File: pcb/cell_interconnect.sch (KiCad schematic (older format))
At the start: 24 parts, among them J1 C0, J10 Taps 6-8, J11 Taps 0-5, J2 C1, J3 C2, J4 C3, J5 C4, J6 C5, J7 C6, J8 C7, J9 C8

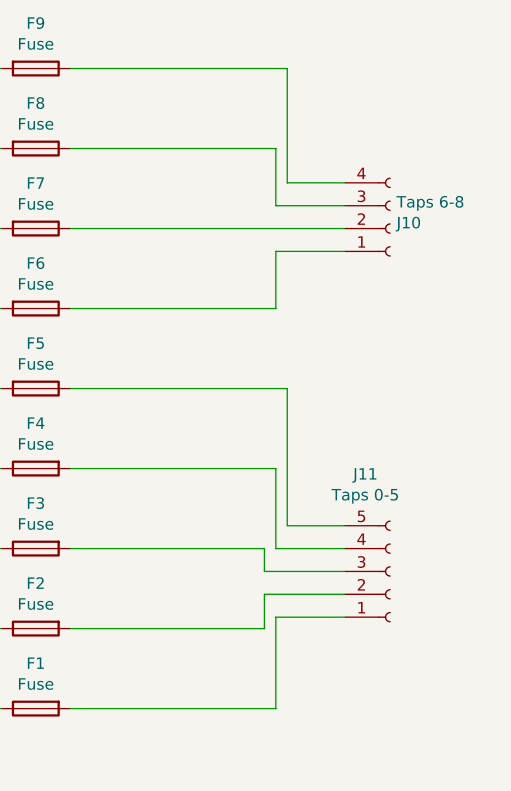
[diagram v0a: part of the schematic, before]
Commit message: AFE mostly complete
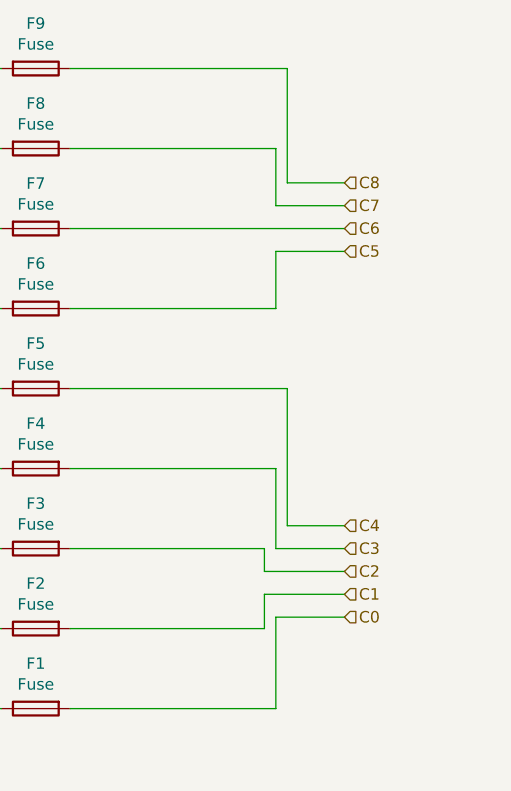
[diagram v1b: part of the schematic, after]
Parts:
- removed J10: Taps 6-8, Connector_PinSocket_2.54mm:PinSocket_1x04_P2.54mm_Vertical, symbol Connector:Conn_01x04_Female
- removed J11: Taps 0-5, Connector_PinSocket_2.54mm:PinSocket_1x05_P2.54mm_Vertical, symbol Connector:Conn_01x05_Female
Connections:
- net C5: now reaches F6.1
- net C6: now reaches F7.1
- net C7: now reaches F8.1
- net C8: now reaches F9.1
- net C0: now reaches F1.2
- net C1: now reaches F2.2
- net C2: now reaches F3.2
- net C3: now reaches F4.2
- net C4: now reaches F5.1
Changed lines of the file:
@@
 $Descr A4 11693 8268
 encoding utf-8
-Sheet 4 4
+Sheet 3 4
 Title ""
 Date ""
@@
 $EndDescr
 $Comp
-L Connector:Conn_01x05_Female J11
-U 1 1 607E756A
-P 6850 4500
-F 0 "J11" H 6742 4075 50  0000 C CNN
-F 1 "Taps 0-5" H 6742 4166 50  0000 C CNN
-F 2 "Connector_PinSocket_2.54mm:PinSocket_1x05_P2.54mm_Vertical" H 6850 4500 50  0001 C CNN
-F 3 "~" H 6850 4500 50  0001 C CNN
-	1    6850 4500
-	1    0    0    1
-$EndComp
-$Comp
 L Connector_Generic:Conn_01x01 J8
 U 1 1 607E9C8D
@@
 	5450 2300 6400 2300
 $Comp
-L Connector:Conn_01x04_Female J10
-U 1 1 607E6DEF
-P 6850 3000
-F 0 "J10" H 6878 2976 50  0000 L CNN
-F 1 "Taps 6-8" H 6878 2885 50  0000 L CNN
-F 2 "Connector_PinSocket_2.54mm:PinSocket_1x04_P2.54mm_Vertical" H 6850 3000 50  0001 C CNN
-F 3 "~" H 6850 3000 50  0001 C CNN
-	1    6850 3000
-	1    0    0    1
-$EndComp
-$Comp
 L Mechanical:MountingHole H1
 U 1 1 60817FDA
@@
 	1    0    0    -1
 $EndComp
+Text HLabel 6650 2800 2    50   Input ~ 0
+C8
+Text HLabel 6650 2900 2    50   Input ~ 0
+C7
+Text HLabel 6650 3000 2    50   Input ~ 0
+C6
+Text HLabel 6650 3100 2    50   Input ~ 0
+C5
+Text HLabel 6650 4300 2    50   Input ~ 0
+C4
+Text HLabel 6650 4400 2    50   Input ~ 0
+C3
+Text HLabel 6650 4500 2    50   Input ~ 0
+C2
+Text HLabel 6650 4600 2    50   Input ~ 0
+C1
+Text HLabel 6650 4700 2    50   Input ~ 0
+C0
 $EndSCHEMATC
